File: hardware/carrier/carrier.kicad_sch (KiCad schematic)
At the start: 7 parts

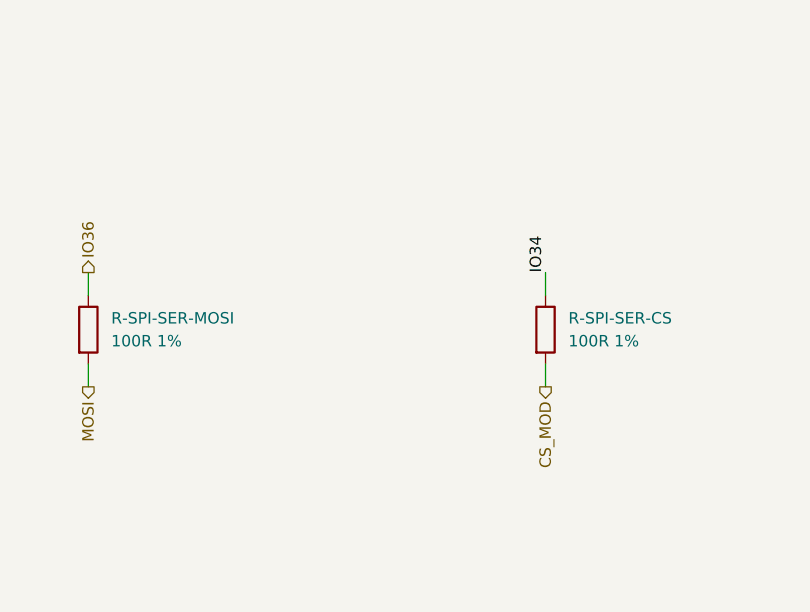
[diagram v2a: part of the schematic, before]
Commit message: Link supervision not restored; CS_MOD pulled up at both ends of the umbilical
Owner, 2026-09-30: "Assume the module will be operating with an umbilical
attached to a controller" - link supervision stays unfitted, recorded on its
page, its notes and ADR 0004; CLR stays tied inactive, OE enabled.

"Fix the SPI pull up": the module's cable-side CS pull-up had its top end on
no net. It is now R-CS-PULL-INST, 10k to 3V3 on the main board's carrier
sheet (IO34 beside J-MCU 13/14, MCU side of R-SPI-SER-CS), and R-PULL-CS at
the module weakened to 100k and taken to LOGIC_5V (row R-CS-PULL-MOD). The
proposed weak pull-DOWN at the module was not fitted: the 74AHCT125 does not
invert, so it would have held SYNC low (selected) with the umbilical out.
spi-link.md tabulates the four link states; GPIO34 is not a strapping pin.

Co-Authored-By: Claude Opus 5.5 <noreply@anthropic.com>
Claude-Session: https://claude.ai/code/session_01LmB4muFXnoLprWX4JzuJ5A
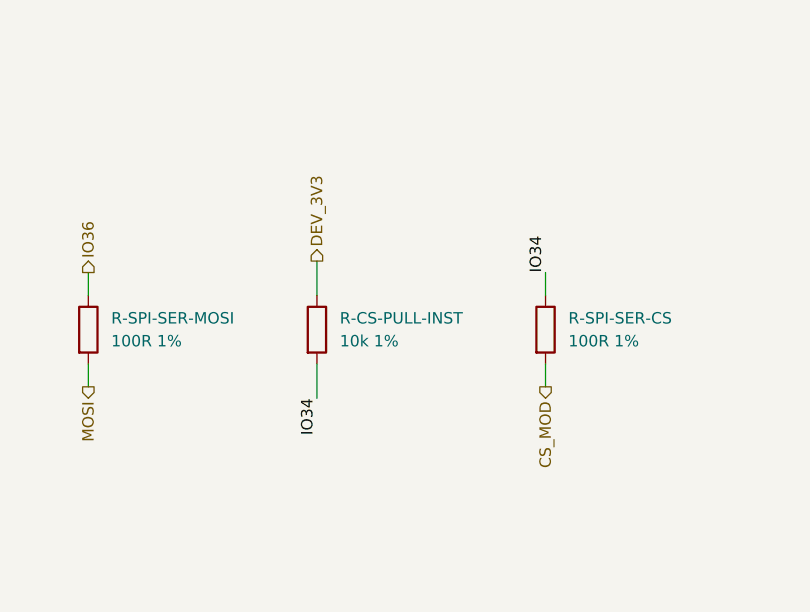
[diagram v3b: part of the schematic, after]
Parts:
- added R-CS-PULL-INST: 10k 1%, Resistor_SMD:R_0805_2012Metric, symbol Device:R
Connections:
- net DEV_3V3: now also R-CS-PULL-INST.1
- net IO34: now also R-CS-PULL-INST.2
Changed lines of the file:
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@@
   (no_connect (at 45.72 274.32))
   (text "FROM THE HAND-WRITTEN NETLIST THIS SHEET REPLACES (verbatim; the part notes are on each part's Note field):\n\nAUTHORITATIVE for connectivity of the CARRIER BOARD ITSELF - the dev board, its connector J-MCU, and the SPI\negress drawn in carrier.md §4. THIS FILE SITS AT hardware/carrier/, not in a circuit directory, because\ncarrier.md is the board page rather than a circuit page: its bom.csv fragment holds the dev board, its ribbon\nand connector, and the PCB, and its drawings show four OTHER circuits' parts for context. THE RIBBON IS NOT A\nCOMPONENT. U-MCU-RT is on the lid and CBL-MCU-RIBBON is soldered to its pad rows and plugged into J-MCU on the\nmain board: one conductor per pad, straight, with no pin map of its own. So each Matrix pin and its J-MCU pin\nare ONE NET here, exactly as interfaces/spi-link treats the umbilical cable. J-MCU's pins are numbered: ribbon\nconductor n is J-MCU pin n, allocated by ADR 0018 (the J-MCU row gives the map). PARALLEL CONDUCTORS ARE\nSEPARATE J-MCU PINS ON ONE NET. Three conductors carry 5V and four carry GND, for current and for the ground\nshift under the ADC's reference (carrier.md, \"The Matrix and the umbilical at the tail end\"). On the Matrix\ntwo of the 5V conductors share the 5V pad, and three of the grounds land on test pad TP3 - so U-MCU-RT.P5V and\nU-MCU-RT.TP2 are both its VCC_5V, and U-MCU-RT.GND and U-MCU-RT.TP3 both its GND. §2's ANALOG FRONT END IS NOT\nHERE. The reference, the buffer, the sensor and the ADC are drawn on this page and owned by\ncarrier/breath-excitation- reference, carrier/breath-adc and interfaces/breath-sense-link. They are declared\n`foreign:` so the drawing stays checkable without this file pretending to own them, and they are netlisted in\ntheir own directories against this page.\n\nto the cluster chain\n\nto the LED strip\n\nto the service header\n\nthe shared SPI host: the ADC on this board, the DAC two metres away\n\nsupply\n\nJ-UMB pin 8 arrives here and is this board's ground (ADR 0018)\n\n--- the shared SPI host, at the MCU pins -------------------------- ONE HOST, TWO DEVICES. The same clock and\ndata reach the MCP3202 on this board and the DAC8568 two metres away; only the chip selects differ. So the MCU\npin and the umbilical conductor are DIFFERENT NETS with the series resistor between them, and the ADC hangs on\nthe MCU side.\n\nLocal: the MCU pin to its series resistor, and nothing else. It crosses no boundary, so it is not in\nhardware/nets.yaml.\n\n--- the cluster chain ---------------------------------------------\n\n--- the LED strip ---------------------------------------------------\n\n--- the service header ----------------------------------------------\n\n--- supply ----------------------------------------------------------\n\nThree conductors: two on the Matrix's 5V pad, one on TP2.\n\nFour conductors: one on the Matrix's GND pad, three on TP3. DIG_GND, J-UMB pin 8 (interfaces/spi-link), ties\nto this board's ground at J-UMB - a short, wide connection at the pin, copper and not a part (ADR 0018). On\nthe board that copper is a net tie, NT-DIG, beside the pin: DIG_GND keeps its name because at the module end\nconductor 8 is its own net, and where it meets AGND_MOD there is dig-gnd-topology, still disputed.\n\n--- reset and boot, to the service header (ADR 0018) ----------------- Pulled up on the Matrix by R8 / R10\n(10k to its 3V3) and pulled down by its buttons. Nothing in series; whatever is on HDR-SERVICE pulls to ground\nonly.\n\n--- the two spare GPIO the ribbon carries ----------------------------- Local: they reach J-MCU and nothing\nelse on this board (two test pads beside it, per the J-MCU row).\n\nThe fourth clamp channel has no fourth signal: J-UMB pin 8 is DIG_GND, which is a return rather than something\nto clamp." (at 256.54 38.099999999999994 0) (effects (font (size 1.27 1.27)) (justify left top)))
+  (symbol (lib_id "Device:R") (at 116.84 233.68 0) (unit 1)
+    (in_bom yes) (on_board yes) (dnp no)
+    (property "Reference" "R-CS-PULL-INST" (at 119.38 232.41 0) (effects (font (size 1.27 1.27)) (justify left)))
+    (property "Value" "10k 1%" (at 119.38 234.95 0) (effects (font (size 1.27 1.27)) (justify left)))
+    (property "Footprint" "Resistor_SMD:R_0805_2012Metric" (at 116.84 233.68 0) (effects (font (size 1.27 1.27)) hide))
+    (property "Datasheet" "" (at 116.84 233.68 0) (effects (font (size 1.27 1.27)) hide))
+    (property "Row" "R-CS-PULL-INST" (at 116.84 233.68 0) (effects (font (size 1.27 1.27)) hide))
+    (property "Pins" "1=1 2=2" (at 116.84 233.68 0) (effects (font (size 1.27 1.27)) hide))
+    (property "Note" "CS_MOD's idle pull-up, AT THE INSTRUMENT END (owner, 2026-09-30: 'Fix the SPI pull up'): IO34 to the dev board's 3V3, on the MCU side of R-SPI-SER-CS, beside J-MCU pins 13 (3V3) and 14 (IO34). IO34 has no pull of its own at reset - 'IE' only [ds ESP32-S3-datasheet-v2.2.pdf p.17] - so this is what holds CS deselected while the ESP32 resets and boots. It is not a strapping pin (GPIO0/3/45/46, p.26). Values and the three link states: interfaces/spi-link/spi-link.md, 'CS_MOD's two pulls'" (at 116.84 233.68 0) (effects (font (size 1.27 1.27)) hide))
+    (property "Pins_source" "a two-terminal resistor" (at 116.84 233.68 0) (effects (font (size 1.27 1.27)) hide))
+    (property "Manufacturer" "UNI-ROYAL(Uniroyal Elec)" (at 116.84 233.68 0) (effects (font (size 1.27 1.27)) hide))
+    (property "MPN" "0805W8F1002T5E" (at 116.84 233.68 0) (effects (font (size 1.27 1.27)) hide))
+    (property "LCSC" "C17414" (at 116.84 233.68 0) (effects (font (size 1.27 1.27)) hide))
+    (property "Assembly" "machine" (at 116.84 233.68 0) (effects (font (size 1.27 1.27)) hide))
+    (pin "1")
+    (pin "2")
+    (instances (project "main-board" (path "/b12a49ac-ffa0-5078-b2ba-e15d161f1936/a85e29d2-c931-5bfb-b9d3-d7fa7fbe8a61" (reference "R40") (unit 1))) (project "carrier" (path "/37c35da0-1428-5d60-8327-f4837789ec8d" (reference "R-CS-PULL-INST") (unit 1))))
+  )
+  (wire (pts (xy 116.84 229.87) (xy 116.84 226.06)) (stroke (width 0) (type default)))
+  (hierarchical_label "DEV_3V3" (shape output) (at 116.84 226.06 90) (effects (font (size 1.27 1.27)) (justify left))
+    (property "Dir" "out" (at 116.84 226.06 0) (effects (font (size 1.27 1.27)) hide))
+    (property "To" "interfaces/key-chain-loom" (at 116.84 226.06 0) (effects (font (size 1.27 1.27)) hide))
+    (property "Figure" "key-pullup-qty" (at 116.84 226.06 0) (effects (font (size 1.27 1.27)) hide)))
+  (wire (pts (xy 116.84 237.49) (xy 116.84 241.3)) (stroke (width 0) (type default)))
+  (label "IO34" (at 116.84 241.3 270) (fields_autoplaced) (effects (font (size 1.27 1.27)) (justify right bottom)))
   (sheet_instances (path "/" (page "1")))
 )
